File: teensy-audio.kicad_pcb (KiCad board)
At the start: 2 copper layers, 80 x 154.4 mm, 63 parts, among them J1 AudioJack3, J10 Conn_02x06_Odd_Even, J11 Conn_02x08_Odd_Even, J12 Barrel_Jack, J13 Conn_01x04, J2 Conn_01x06, J3 Conn_01x04, J4 Conn_02x05_Odd_Even, J5 AudioJack3, J6 Conn_01x04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

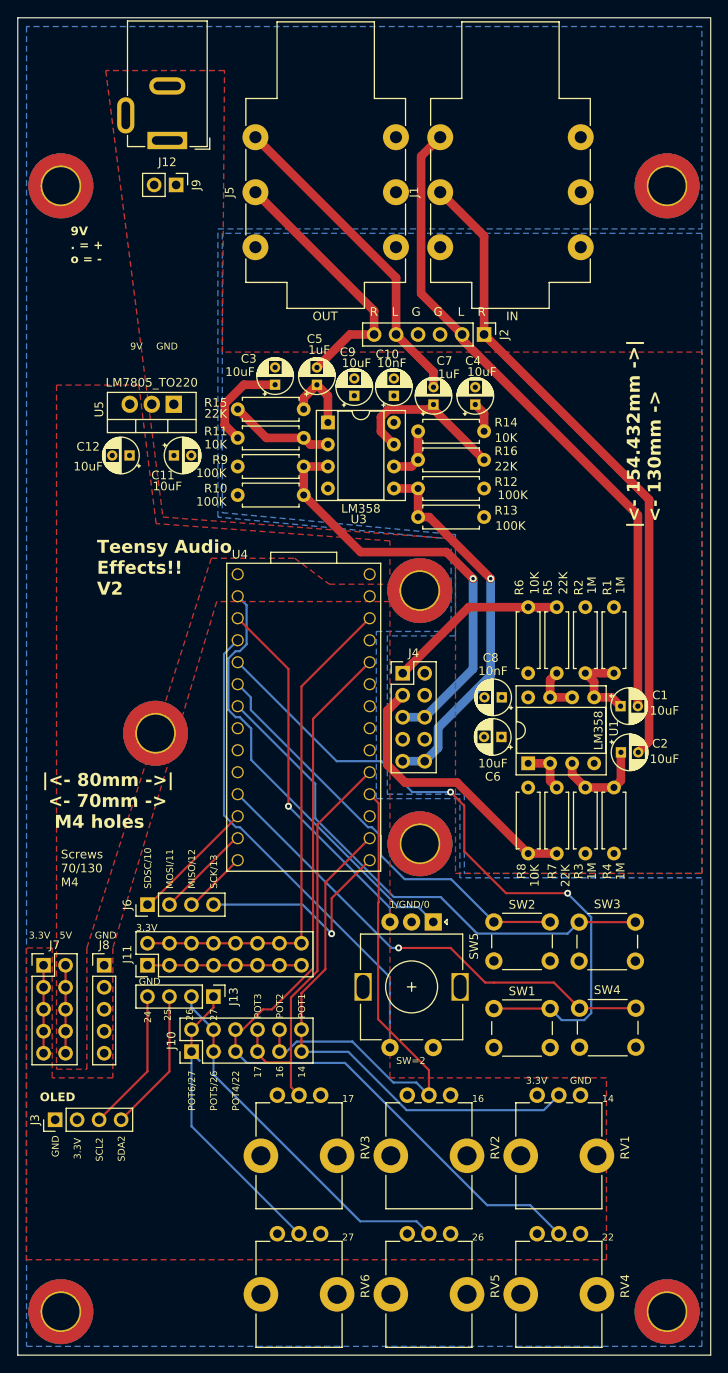
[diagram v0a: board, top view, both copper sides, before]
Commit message: do not stack teensy and teensy audio
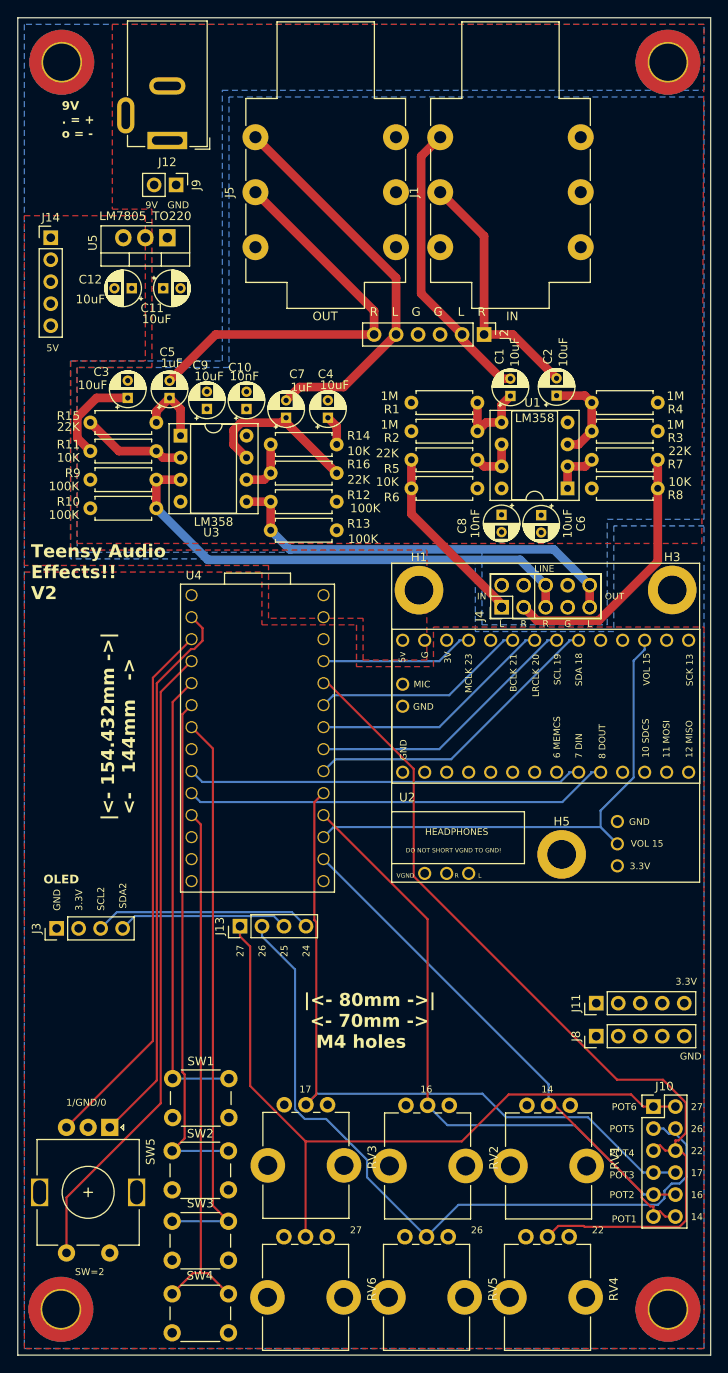
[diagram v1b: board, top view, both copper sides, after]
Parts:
- removed J6: Conn_01x04, Connector_PinHeader_2.54mm:PinHeader_1x04_P2.54mm_Vertical
- removed J7: Conn_02x05_Odd_Even, Connector_PinHeader_2.54mm:PinHeader_2x05_P2.54mm_Vertical
- added J14: Conn_01x05, Connector_PinHeader_2.54mm:PinHeader_1x05_P2.54mm_Vertical, F.Cu at (69.8, 64.3)
- added U2: Teensy4.0_AudioShield_REVD, teensy_audio_shield:4.0audioshield, F.Cu at (110.5, 126.0)
- H1, H3, H5: footprint MountingHole:MountingHole_4.3mm_M4_DIN965_Pad_TopBottom -> MountingHole:MountingHole_3.2mm_M3_DIN965_Pad_TopBottom
- J11: value Conn_02x08_Odd_Even -> Conn_01x05; footprint Connector_PinHeader_2.54mm:PinHeader_2x08_P2.54mm_Vertical -> Connector_PinHeader_2.54mm:PinHeader_1x05_P2.54mm_Vertical
- moved SW3 58.3 mm to (90.4, 182.3)
- moved SW4 57.5 mm to (90.4, 190.7)
- moved J8 57.4 mm to (132.8, 156.5), turned to 90 degrees
- moved J10 53.7 mm to (139.4, 164.6), turned to 0 degrees
- moved J11 52.0 mm to (132.8, 152.7)
- moved R3 49.5 mm to (139.9, 86.6), turned to 180 degrees
- moved SW2 45.6 mm to (83.9, 169.7)
- moved R8 44.7 mm to (139.9, 93.2), turned to 180 degrees
- moved R4 44.5 mm to (132.3, 83.3), turned to 0 degrees
- moved SW5 44.2 mm to (76.7, 167.0)
- moved C2 41.9 mm to (128.3, 82.5), turned to 90 degrees
- moved R7 38.1 mm to (132.3, 89.9), turned to 0 degrees
- moved C1 38.0 mm to (122.9, 82.5), turned to 90 degrees
- moved SW1 38.0 mm to (83.9, 161.4)
- moved H1 34.6 mm to (112.4, 105.0)
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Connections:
- J11 pad 1: GND -> +3.3V
- J11 pad 3: GND -> +3.3V
- J11 pad 5: GND -> +3.3V
- U4 pad 12: SDCS -> unconnected-(U4-10_CS_MQSR-Pad12)
- U4 pad 13: MOSI -> unconnected-(U4-11_MOSI_CTX1-Pad13)
- U4 pad 14: MISO -> unconnected-(U4-12_MISO_MQSL-Pad14)
- U4 pad 20: SCK -> unconnected-(U4-13_SCK_CRX1_LED-Pad20)
- U4 pad 8: MEMCS -> unconnected-(U4-6_OUT1D-Pad8)
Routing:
- net +3.3V: track 73.2 -> 0.00 mm
- net VOL: track 0.00 -> 58.9 mm
- net POT6: track 35.0 -> 84.5 mm
- net DOUT: track 0.00 -> 49.2 mm
- net JACK_IN_R: track 75.2 -> 29.0 mm
- net DIN: track 0.00 -> 45.8 mm
- net POT5: track 43.4 -> 87.4 mm
- net JACK_IN_L: track 77.2 -> 33.9 mm
- net SDA: track 0.00 -> 35.8 mm
- net POT3: track 48.5 -> 84.0 mm
- net SCL: track 0.00 -> 32.2 mm
- net LRCLK: track 0.00 -> 28.6 mm
- net SW2: track 79.3 -> 53.1 mm, vias 2 -> 0
- net SCK: track 25.3 -> 0.00 mm, vias 1 -> 0
- net BCLK: track 0.00 -> 25.0 mm
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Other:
- board text added: "POT4"
- board text added: "POT5"
- board text added: "POT6"
- board text added: "|<- 154.432mm ->| <- 144mm ->"
- board text removed: "MISO/12"
- board text removed: "MOSI/11"
- board text removed: "POT4/22"
- board text removed: "POT5/26"
- board text removed: "POT6/27"
- board text removed: "SCK/13"
- board text removed: "SDSC/10"
- board text removed: "Screws 70/130 M4"
- board text removed: "|<- 154.432mm ->| <- 130mm ->"

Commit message: cleanup of PCB (cosmetic)
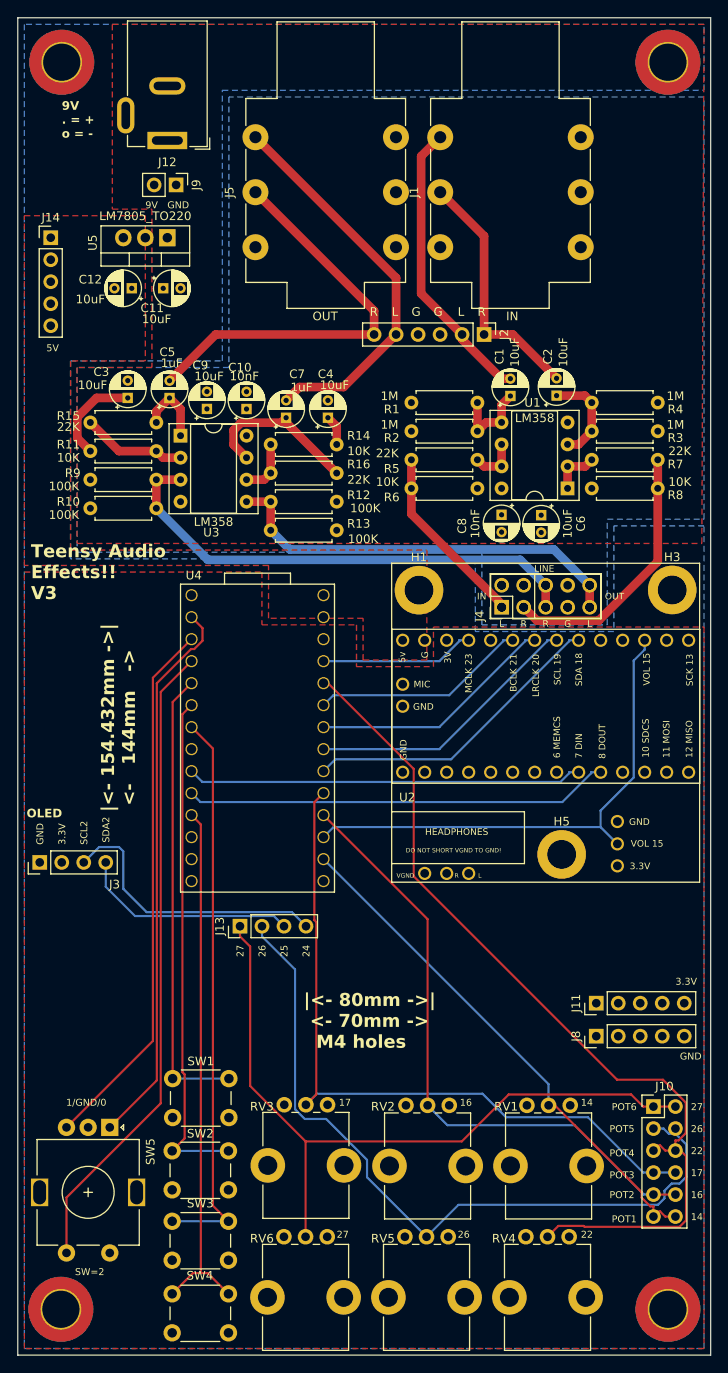
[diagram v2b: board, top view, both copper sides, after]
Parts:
- moved J3 7.87 mm to (68.6, 136.4)
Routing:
- net SCL2: track 25.2 -> 32.7 mm
- net SDA2: track 19.7 -> 25.3 mm
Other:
- board text added: "Teensy Audio Effects!! V3"
- board text removed: "Teensy Audio Effects!! V2"
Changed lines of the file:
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@@
   )
   (footprint "Connector_PinHeader_2.54mm:PinHeader_1x04_P2.54mm_Vertical" (layer "F.Cu")
-    (at 70.53155 144.018 90)
+    (at 68.58 136.398 90)
     (descr "Through hole straight pin header, 1x04, 2.54mm pitch, single row")
     (tags "Through hole pin header THT 1x04 2.54mm single row")
@@
     (property "ki_keywords" "connector")
     (attr through_hole)
-    (fp_text reference "J3" (at 0 -2.33 90) (layer "F.SilkS")
+    (fp_text reference "J3" (at -2.54 8.636 180) (layer "F.SilkS")
         (effects (font (size 1 1) (thickness 0.15)))
     )
@@
     (property "ki_keywords" "resistor variable")
     (attr through_hole)
-    (fp_text reference "RV1" (at 6.05 -10.15 90) (layer "F.SilkS")
+    (fp_text reference "RV1" (at 0.142 2.408 -180) (layer "F.SilkS")
         (effects (font (size 1 1) (thickness 0.15)))
     )
@@
     (property "ki_keywords" "resistor variable")
     (attr through_hole)
-    (fp_text reference "RV2" (at 6.05 -10.15 90) (layer "F.SilkS")
+    (fp_text reference "RV2" (at 0.142 2.662 -180) (layer "F.SilkS")
         (effects (font (size 1 1) (thickness 0.15)))
     )
@@
     (property "ki_keywords" "resistor variable")
     (attr through_hole)
-    (fp_text reference "RV3" (at 6.05 -10.15 90) (layer "F.SilkS")
+    (fp_text reference "RV3" (at 0.208 2.58 -180) (layer "F.SilkS")
         (effects (font (size 1 1) (thickness 0.15)))
     )
@@
     (property "ki_keywords" "resistor variable")
     (attr through_hole)
-    (fp_text reference "RV4" (at 6.05 -10.15 90) (layer "F.SilkS")
+    (fp_text reference "RV4" (at 0.208 2.54 -180) (layer "F.SilkS")
         (effects (font (size 1 1) (thickness 0.15)))
     )
@@
     (property "ki_keywords" "resistor variable")
     (attr through_hole)
-    (fp_text reference "RV6" (at 6.05 -10.15 90) (layer "F.SilkS")
+    (fp_text reference "RV6" (at 0.208 2.54 -180) (layer "F.SilkS")
         (effects (font (size 1 1) (thickness 0.15)))
     )
@@
     (property "ki_keywords" "resistor variable")
     (attr through_hole)
-    (fp_text reference "RV5" (at 6.05 -10.15 90) (layer "F.SilkS")
+    (fp_text reference "RV5" (at 0.208 2.54 -180) (layer "F.SilkS")
         (effects (font (size 1 1) (thickness 0.15)))
     )
@@
   (gr_rect (start 66.04 38.862) (end 146.05 193.294)
     (stroke (width 0.1) (type default)) (fill none) (layer "Edge.Cuts"))
-  (gr_text "GND" (at 71.03955 141.986 90) (layer "F.SilkS")
+  (gr_text "GND" (at 69.088 134.366 90) (layer "F.SilkS")
     (effects (font (size 0.8 0.8) (thickness 0.08)) (justify left bottom))
   )
@@
     (effects (font (size 0.8 0.8) (thickness 0.08)) (justify left bottom))
   )
-  (gr_text "OLED" (at 69.00755 138.938) (layer "F.SilkS")
+  (gr_text "OLED" (at 67.056 131.318) (layer "F.SilkS")
     (effects (font (size 1 1) (thickness 0.16) bold) (justify left bottom))
   )
@@
     (effects (font (size 1 1) (thickness 0.15)) (justify left bottom))
   )
-  (gr_text "26" (at 118.364 179.324) (layer "F.SilkS")
+  (gr_text "26" (at 116.84 179.832) (layer "F.SilkS")
     (effects (font (size 0.8 0.8) (thickness 0.08)) (justify left bottom))
   )
@@
     (effects (font (size 1 1) (thickness 0.15)) (justify left bottom))
   )
-  (gr_text "Teensy Audio\nEffects!!\nV2" (at 67.564 106.172) (layer "F.SilkS")
+  (gr_text "Teensy Audio\nEffects!!\nV3" (at 67.564 106.172) (layer "F.SilkS")
     (effects (font (size 1.5 1.5) (thickness 0.3) bold) (justify left bottom))
   )
@@
     (effects (font (size 0.8 0.8) (thickness 0.08)) (justify left bottom))
   )
-  (gr_text "14" (at 126.492 163.068) (layer "F.SilkS")
+  (gr_text "14" (at 131.064 164.592) (layer "F.SilkS")
     (effects (font (size 0.8 0.8) (thickness 0.08)) (justify left bottom))
   )
@@
     (effects (font (size 1 1) (thickness 0.15)) (justify left bottom))
   )
-  (gr_text "27" (at 104.394 179.324) (layer "F.SilkS")
+  (gr_text "27" (at 102.87 179.832) (layer "F.SilkS")
     (effects (font (size 0.8 0.8) (thickness 0.08)) (justify left bottom))
   )
@@
     (effects (font (size 0.8 0.8) (thickness 0.08)) (justify left bottom))
   )
-  (gr_text "22" (at 132.334 179.324) (layer "F.SilkS")
+  (gr_text "22" (at 131.064 179.832) (layer "F.SilkS")
     (effects (font (size 0.8 0.8) (thickness 0.08)) (justify left bottom))
   )
-  (gr_text "|<- 154.432mm ->|\n <-   144mm   ->" (at 79.756 131.572 90) (layer "F.SilkS")
+  (gr_text "|<- 154.432mm ->|\n <-   144mm   ->" (at 79.756 130.556 90) (layer "F.SilkS")
     (effects (font (size 1.5 1.5) (thickness 0.25) bold) (justify left bottom))
   )
@@
     (effects (font (size 0.8 0.8) (thickness 0.08)) (justify left bottom))
   )
-  (gr_text "SDA2" (at 78.65955 141.732 90) (layer "F.SilkS")
+  (gr_text "SDA2" (at 76.708 134.112 90) (layer "F.SilkS")
     (effects (font (size 0.8 0.8) (thickness 0.08)) (justify left bottom))
   )
@@
     (effects (font (size 1 1) (thickness 0.2) bold) (justify left bottom))
   )
-  (gr_text "3.3V" (at 73.57955 141.986 90) (layer "F.SilkS")
+  (gr_text "3.3V" (at 71.628 134.366 90) (layer "F.SilkS")
     (effects (font (size 0.8 0.8) (thickness 0.08)) (justify left bottom))
   )
@@
     (effects (font (size 0.8 0.8) (thickness 0.08)) (justify left bottom))
   )
-  (gr_text "17" (at 98.552 163.068) (layer "F.SilkS")
+  (gr_text "17" (at 103.124 164.592) (layer "F.SilkS")
     (effects (font (size 0.8 0.8) (thickness 0.08)) (justify left bottom))
   )
@@
     (effects (font (size 1 1) (thickness 0.15)) (justify left bottom))
   )
-  (gr_text "SCL2" (at 76.11955 141.986 90) (layer "F.SilkS")
+  (gr_text "SCL2" (at 74.168 134.366 90) (layer "F.SilkS")
     (effects (font (size 0.8 0.8) (thickness 0.08)) (justify left bottom))
   )
@@
     (effects (font (size 0.8 0.8) (thickness 0.08)) (justify left bottom))
   )
-  (gr_text "16" (at 112.522 163.068) (layer "F.SilkS")
+  (gr_text "16" (at 117.094 164.592) (layer "F.SilkS")
     (effects (font (size 0.8 0.8) (thickness 0.08)) (justify left bottom))
   )
@@
   (segment (start 88.9 75.438) (end 83.566 80.772) (width 1) (layer "F.Cu") (net 34))
   (segment (start 107.188 72.708) (end 93.485 59.005) (width 1) (layer "F.Cu") (net 34))
-  (segment (start 79.58055 142.589) (end 78.15155 144.018) (width 0.25) (layer "B.Cu") (net 37))
+  (segment (start 79.58055 142.589) (end 76.2 139.20845) (width 0.25) (layer "B.Cu") (net 37))
   (segment (start 96.784 143.764) (end 95.609 142.589) (width 0.25) (layer "B.Cu") (net 37))
+  (segment (start 76.2 139.20845) (end 76.2 136.398) (width 0.25) (layer "B.Cu") (net 37))
   (segment (start 95.609 142.589) (end 79.58055 142.589) (width 0.25) (layer "B.Cu") (net 37))
-  (segment (start 77.49055 142.139) (end 75.61155 144.018) (width 0.25) (layer "B.Cu") (net 38))
-  (segment (start 97.699 142.139) (end 77.49055 142.139) (width 0.25) (layer "B.Cu") (net 38))
+  (segment (start 77.724 134.62) (end 75.438 134.62) (width 0.25) (layer "B.Cu") (net 38))
+  (segment (start 97.699 142.139) (end 80.925 142.139) (width 0.25) (layer "B.Cu") (net 38))
+  (segment (start 78.232 139.446) (end 78.232 135.128) (width 0.25) (layer "B.Cu") (net 38))
+  (segment (start 78.232 135.128) (end 77.724 134.62) (width 0.25) (layer "B.Cu") (net 38))
   (segment (start 99.324 143.764) (end 97.699 142.139) (width 0.25) (layer "B.Cu") (net 38))
+  (segment (start 75.438 134.62) (end 73.66 136.398) (width 0.25) (layer "B.Cu") (net 38))
+  (segment (start 80.925 142.139) (end 78.232 139.446) (width 0.25) (layer "B.Cu") (net 38))
   (segment (start 119.116 83.302) (end 119.116 86.604) (width 1) (layer "F.Cu") (net 40))
   (segment (start 121.91 85.588) (end 121.91 83.556) (width 1) (layer "F.Cu") (net 40))
